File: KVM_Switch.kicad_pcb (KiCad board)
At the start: 4 copper layers, 100 x 70 mm, 115 parts, among them J1 HDMI_A, J2 HDMI_A, J3 HDMI_A, J4 USB_C_Receptacle_USB2.0_16P, J5 USB_C_Receptacle_USB2.0_16P, J6 USB_C_Receptacle_USB2.0_16P, J7 USB_A_Stacked, J8 USB_A_Stacked, SW1 SPST-NO, U1 TPD4E02B04DQA, U10 USBLC6-2SC6, U11 TS3USB221AQRSERQ1, U12 USBLC6-2SC6, U13 USB2514B_Bi, U14 USBLC6-2SC6, U15 USBLC6-2SC6, U16 USBLC6-2SC6, U17 USBLC6-2SC6, U2 TPD4E02B04DQA, U3 HD3SS215RTQR, U4 TPD4E02B04DQA, U5 TPD4E02B04DQA, U6 TPD4E02B04DQA, U7 TPD4E02B04DQA, U8 TLV75533PDBV, U9 STM32C031G6Ux, X1 24MHz

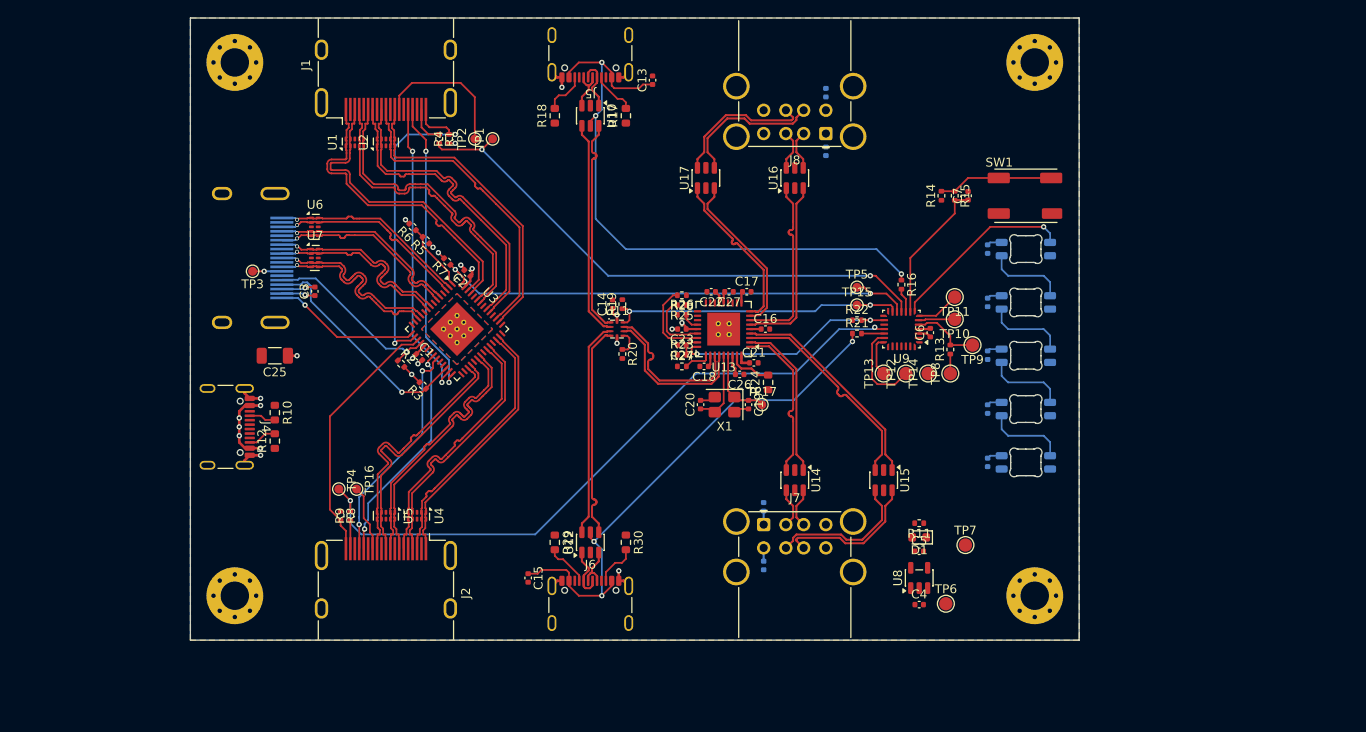
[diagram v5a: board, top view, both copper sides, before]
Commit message: VBUS and +3V3 zones routing
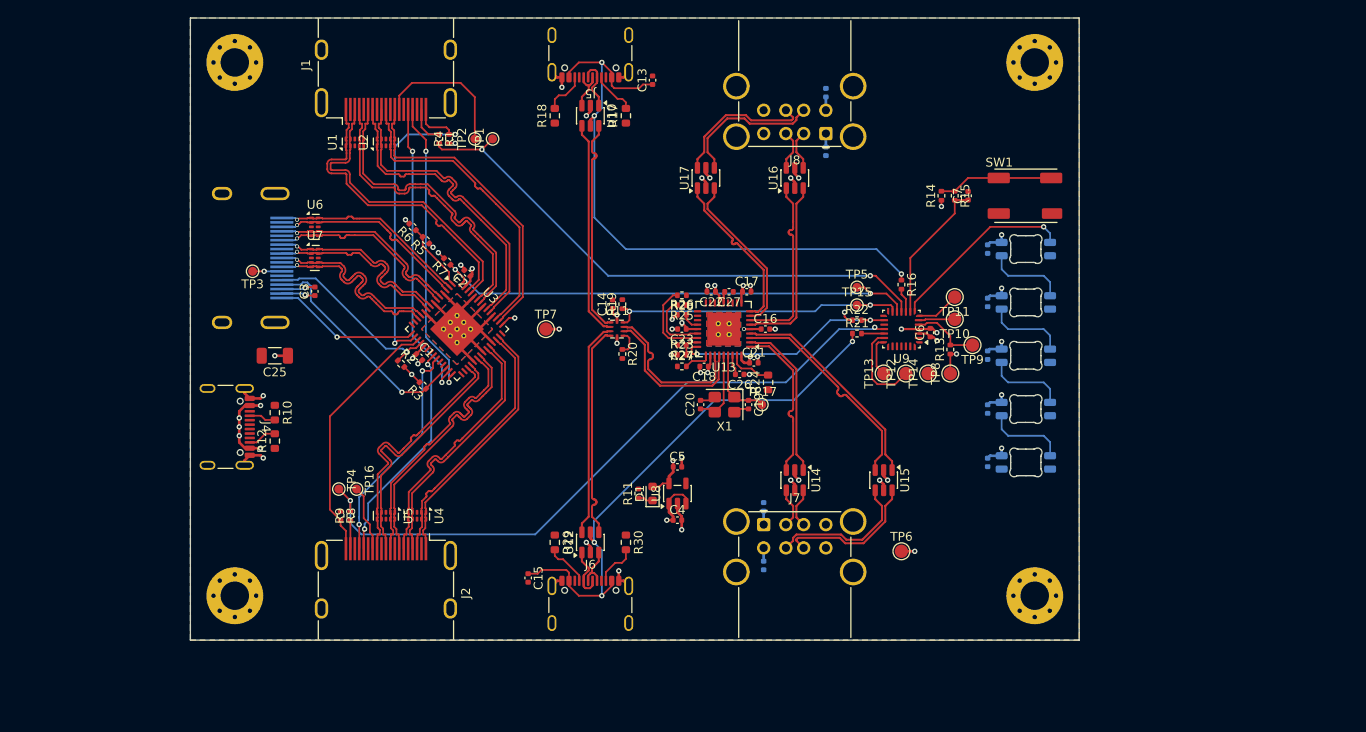
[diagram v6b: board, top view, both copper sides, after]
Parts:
- moved TP7 53.1 mm to (140.0, 100.0)
- moved R11 31.8 mm to (150.4, 118.5), turned to 90 degrees
- moved D1 30.4 mm to (152.0, 118.5), turned to 90 degrees
- moved C4 28.8 mm to (154.8, 121.5)
- moved C5 28.8 mm to (154.8, 115.5)
- moved U8 28.8 mm to (154.8, 118.5)
- moved TP6 7.73 mm to (180.0, 125.0)
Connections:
- J7 pad 8: Net-(J7-GND2) -> GND
- J7 pad SH: Net-(J7-GND2) -> GND
- J8 pad 8: Net-(J8-GND2) -> GND
- J8 pad SH: Net-(J8-GND2) -> GND
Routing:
- net GND: track 26.5 -> 73.5 mm, vias 12 -> 29
- net VBUS: track 27.8 -> 71.0 mm, vias 8 -> 19
- net +3V3: track 19.8 -> 36.2 mm, vias 5 -> 18
- net Net-(D1-K): track 0.00 -> 1.71 mm
- net Net-(U12-VBUS): track 59.9 -> 61.3 mm
- added copper zone on In2.Cu, net +3V3
- added copper zone on In2.Cu, net GND
- added copper zone on In2.Cu, net VBUS

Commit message: Fighting with DRC
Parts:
- D2, D3, D4, D5, D6: footprint LED_SMD:LED_SK6812MINI-E_3.2x2.8mm_P1.5mm_ReverseMount -> KVM_Swtich:LED_SK6812MINI-E_3.2x2.8mm_P1.5mm_ReverseMount
- moved TP17 0.20 mm to (164.5, 108.5)
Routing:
- net GND: track 73.5 -> 115.5 mm, vias 29 -> 53
- net /HDMI_Switch/HDMI_IN_B/HPD: track 29.1 -> 29.8 mm

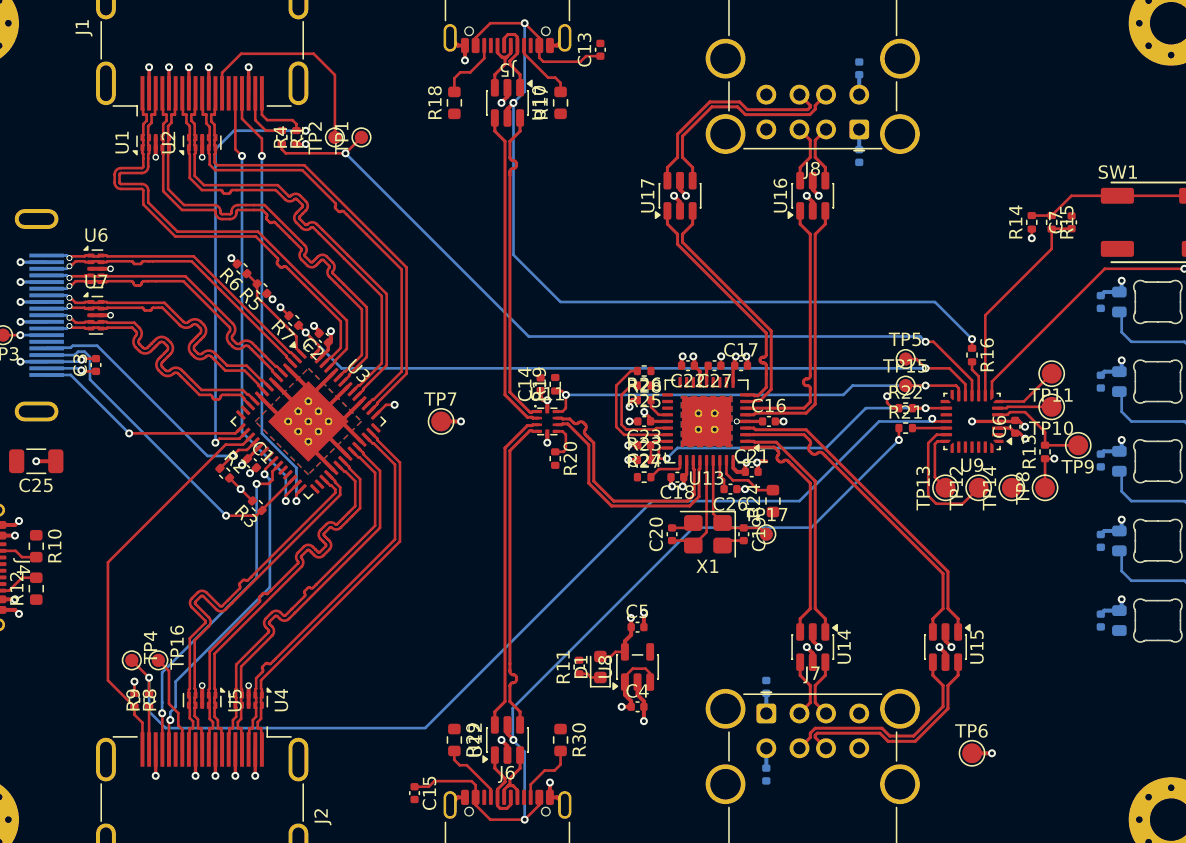
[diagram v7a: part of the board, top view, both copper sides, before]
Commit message: Added ESD protection for the remaining HDMI pins - Not routed yet
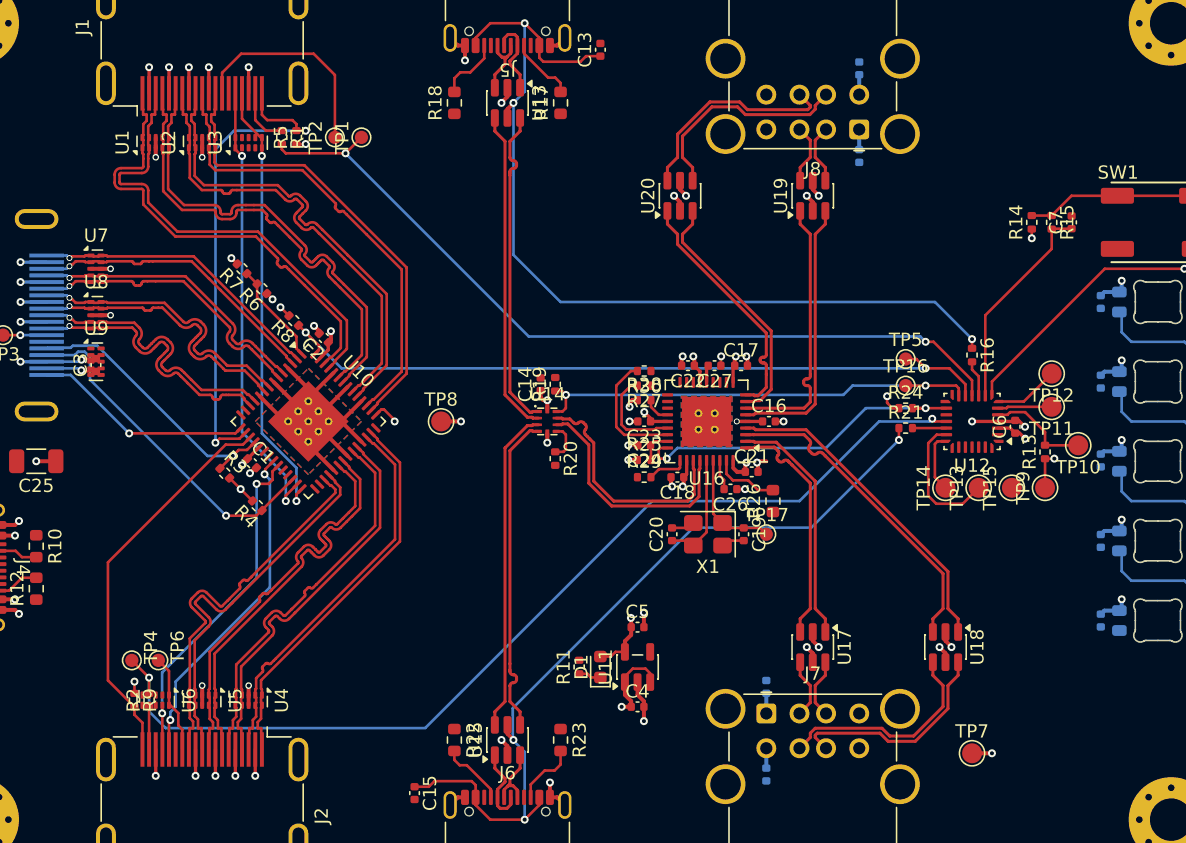
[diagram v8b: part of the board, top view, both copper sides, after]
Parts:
- added U3: TPD4E02B04DQA, Package_SON:USON-10_2.5x1.0mm_P0.5mm, F.Cu at (125.5, 79.0)
- added U6: TPD4E02B04DQA, Package_SON:USON-10_2.5x1.0mm_P0.5mm, F.Cu at (118.5, 121.0)
- added U9: TPD4E02B04DQA, Package_SON:USON-10_2.5x1.0mm_P0.5mm, F.Cu at (114.0, 95.5)
- renumbered R9 to R2, R29 to R22, R30 to R23, R22 to R24, R23 to R25, R24 to R26, R25 to R27, R26 to R28, R27 to R29, R2 to R3, R28 to R30, R3 to R4, R4 to R5, R5 to R6, R6 to R7, R7 to R8, R8 to R9, TP9 to TP10, TP10 to TP11, TP11 to TP12, TP12 to TP13, TP13 to TP14, TP14 to TP15, TP15 to TP16, TP16 to TP6, TP6 to TP7, TP7 to TP8, TP8 to TP9, U3 to U10, U8 to U11, U9 to U12, U10 to U13, U11 to U14, U12 to U15, U13 to U16, U14 to U17, U15 to U18, U16 to U19, U17 to U20, U6 to U7, U7 to U8
